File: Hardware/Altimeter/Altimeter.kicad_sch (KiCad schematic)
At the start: 18 parts, among them J1 Conn_01x06, U1 MS580301BA01-00, U2 MS580301BA01-00, U3 NUP4202

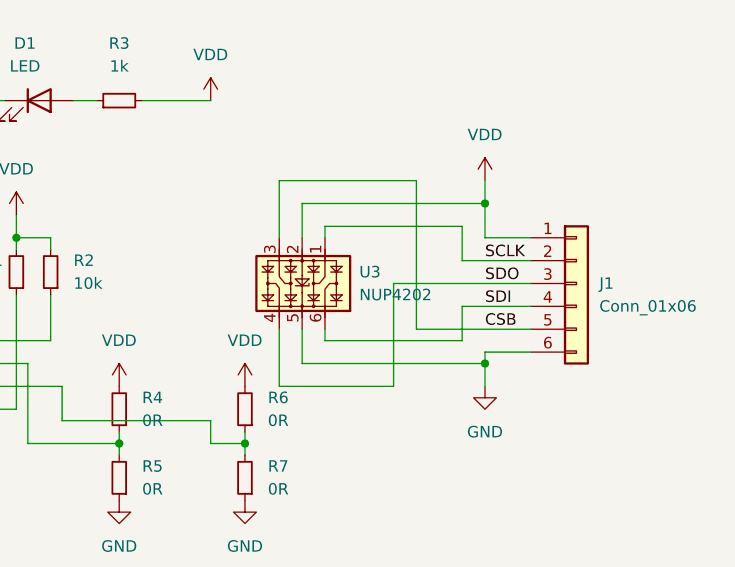
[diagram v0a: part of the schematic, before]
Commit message: Finished the layout for altimeter
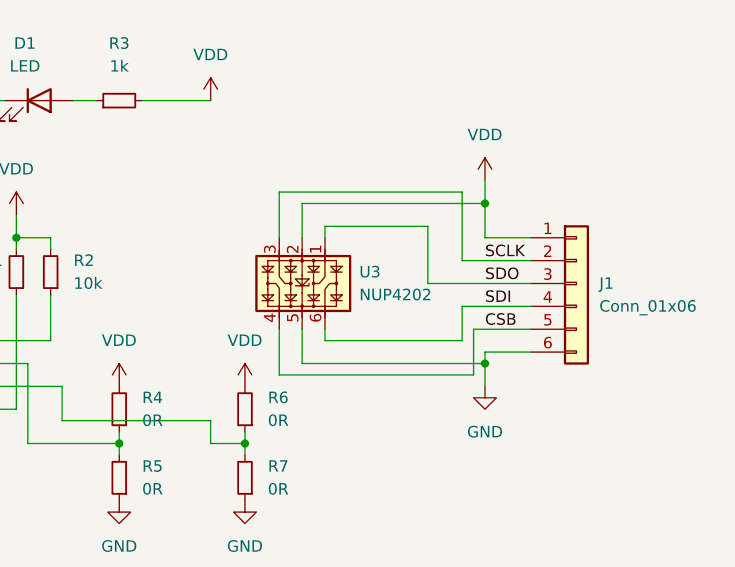
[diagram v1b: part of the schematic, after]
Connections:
- net CSB: now also U3.4; no longer U3.3
- net SCLK: now also U3.3; no longer U3.1
- net SDO: now also U3.1; no longer U3.4
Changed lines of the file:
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@@
-    (stroke (width 0) (type default) (color 0 0 0 0))
-  )
-  (wire (pts (xy 153.67 92.71) (xy 140.97 92.71))
     (stroke (width 0) (type default) (color 0 0 0 0))
   )
@@
     (stroke (width 0) (type default) (color 0 0 0 0))
   )
-  (wire (pts (xy 140.97 92.71) (xy 140.97 86.36))
+  (wire (pts (xy 116.84 92.71) (xy 116.84 96.52))
     (stroke (width 0) (type default) (color 0 0 0 0))
   )
-  (wire (pts (xy 116.84 92.71) (xy 116.84 96.52))
+  (wire (pts (xy 162.56 86.36) (xy 162.56 91.44))
     (stroke (width 0) (type default) (color 0 0 0 0))
   )
@@
     (stroke (width 0) (type default) (color 0 0 0 0))
   )
-  (wire (pts (xy 153.67 81.28) (xy 153.67 92.71))
-    (stroke (width 0) (type default) (color 0 0 0 0))
-  )
   (wire (pts (xy 80.01 106.68) (xy 86.36 106.68))
     (stroke (width 0) (type default) (color 0 0 0 0))
@@
   )
   (wire (pts (xy 123.19 100.33) (xy 123.19 99.06))
+    (stroke (width 0) (type default) (color 0 0 0 0))
+  )
+  (wire (pts (xy 140.97 71.12) (xy 140.97 76.2))
     (stroke (width 0) (type default) (color 0 0 0 0))
   )
@@
     (stroke (width 0) (type default) (color 0 0 0 0))
   )
-  (wire (pts (xy 161.29 78.74) (xy 161.29 74.93))
+  (wire (pts (xy 161.29 71.12) (xy 161.29 78.74))
     (stroke (width 0) (type default) (color 0 0 0 0))
   )
@@
     (stroke (width 0) (type default) (color 0 0 0 0))
   )
+  (wire (pts (xy 162.56 86.36) (xy 168.91 86.36))
+    (stroke (width 0) (type default) (color 0 0 0 0))
+  )
   (wire (pts (xy 115.57 77.47) (xy 115.57 76.2))
     (stroke (width 0) (type default) (color 0 0 0 0))
@@
     (stroke (width 0) (type default) (color 0 0 0 0))
   )
-  (wire (pts (xy 156.21 69.85) (xy 140.97 69.85))
+  (wire (pts (xy 133.35 60.96) (xy 125.73 60.96))
     (stroke (width 0) (type default) (color 0 0 0 0))
   )
-  (wire (pts (xy 133.35 60.96) (xy 125.73 60.96))
+  (wire (pts (xy 161.29 71.12) (xy 140.97 71.12))
     (stroke (width 0) (type default) (color 0 0 0 0))
   )
@@
     (stroke (width 0) (type default) (color 0 0 0 0))
   )
-  (wire (pts (xy 153.67 81.28) (xy 168.91 81.28))
-    (stroke (width 0) (type default) (color 0 0 0 0))
-  )
   (wire (pts (xy 133.35 99.06) (xy 137.16 99.06))
     (stroke (width 0) (type default) (color 0 0 0 0))
   )
   (wire (pts (xy 123.19 97.79) (xy 123.19 99.06))
-    (stroke (width 0) (type default) (color 0 0 0 0))
-  )
-  (wire (pts (xy 161.29 74.93) (xy 146.05 74.93))
     (stroke (width 0) (type default) (color 0 0 0 0))
   )
@@
     (stroke (width 0) (type default) (color 0 0 0 0))
   )
+  (wire (pts (xy 157.48 74.93) (xy 146.05 74.93))
+    (stroke (width 0) (type default) (color 0 0 0 0))
+  )
   (wire (pts (xy 78.74 96.52) (xy 78.74 100.33))
     (stroke (width 0) (type default) (color 0 0 0 0))
   )
   (wire (pts (xy 96.52 92.71) (xy 116.84 92.71))
+    (stroke (width 0) (type default) (color 0 0 0 0))
+  )
+  (wire (pts (xy 140.97 91.44) (xy 140.97 86.36))
     (stroke (width 0) (type default) (color 0 0 0 0))
   )
@@
   )
   (wire (pts (xy 100.33 106.68) (xy 100.33 100.33))
-    (stroke (width 0) (type default) (color 0 0 0 0))
-  )
-  (wire (pts (xy 168.91 86.36) (xy 156.21 86.36))
     (stroke (width 0) (type default) (color 0 0 0 0))
   )
@@
     (stroke (width 0) (type default) (color 0 0 0 0))
   )
+  (wire (pts (xy 157.48 81.28) (xy 157.48 74.93))
+    (stroke (width 0) (type default) (color 0 0 0 0))
+  )
   (wire (pts (xy 105.41 60.96) (xy 110.49 60.96))
     (stroke (width 0) (type default) (color 0 0 0 0))
@@
     (stroke (width 0) (type default) (color 0 0 0 0))
   )
-  (wire (pts (xy 156.21 86.36) (xy 156.21 69.85))
-    (stroke (width 0) (type default) (color 0 0 0 0))
-  )
-  (wire (pts (xy 140.97 69.85) (xy 140.97 76.2))
+  (wire (pts (xy 162.56 91.44) (xy 140.97 91.44))
     (stroke (width 0) (type default) (color 0 0 0 0))
   )
@@
     (stroke (width 0) (type default) (color 0 0 0 0))
   )
+  (wire (pts (xy 168.91 81.28) (xy 157.48 81.28))
+    (stroke (width 0) (type default) (color 0 0 0 0))
+  )
